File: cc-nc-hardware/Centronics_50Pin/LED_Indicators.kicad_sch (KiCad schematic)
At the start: 6 parts, among them U8 74HC14

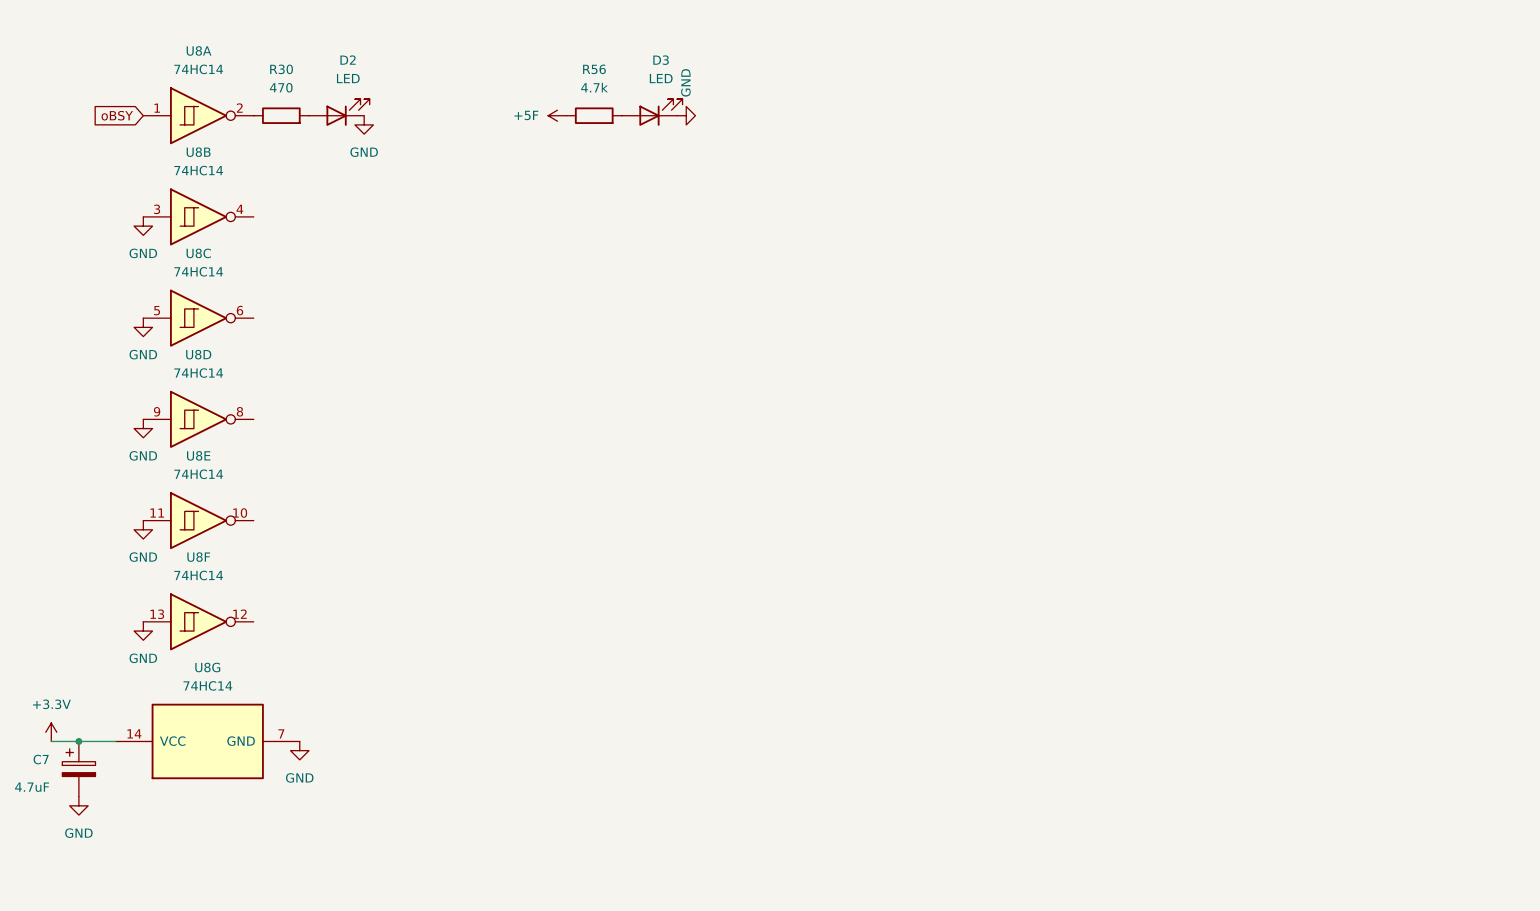
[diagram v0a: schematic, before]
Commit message: New version of C50, shorter and with options for voltage regulator
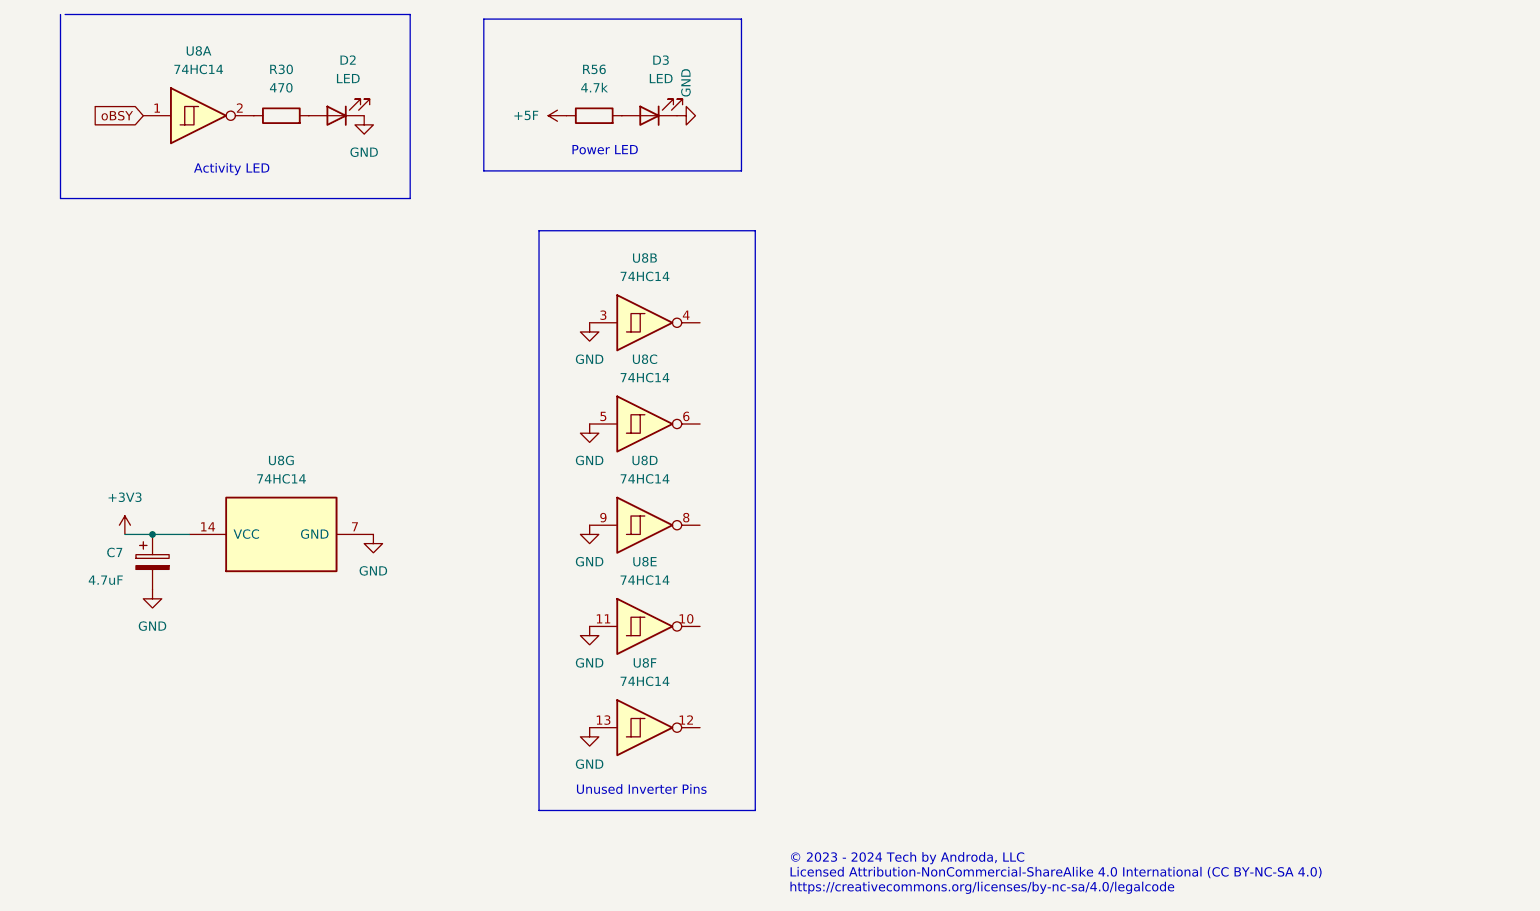
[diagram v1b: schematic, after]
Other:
- note added: "Activity LED"
- note added: "Power LED"
- note added: "Unused Inverter Pins"
- note added: "© 2023 - 2024 Tech by Androda, LLC Licensed Attribution-NonCommercial-ShareAlike 4.0 International (CC BY-NC-SA 4.0) https://creativecommons.org/licenses/by-nc-sa/4.0/legalcode"
- company: (none) -> Tech by Androda, LLC
- title: (none) -> BlueSCSI V2, Centronics 50 Pin, 2024.03a
- moved on the sheet: C7, U8B, U8C, U8D, U8E, U8F, U8G
